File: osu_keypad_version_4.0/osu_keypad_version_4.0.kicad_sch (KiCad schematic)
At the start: 28 parts, among them J1 AVR-ISP-6, SW1 SW_Push, U1 ATmega32U4-A, Y1 16Mhz

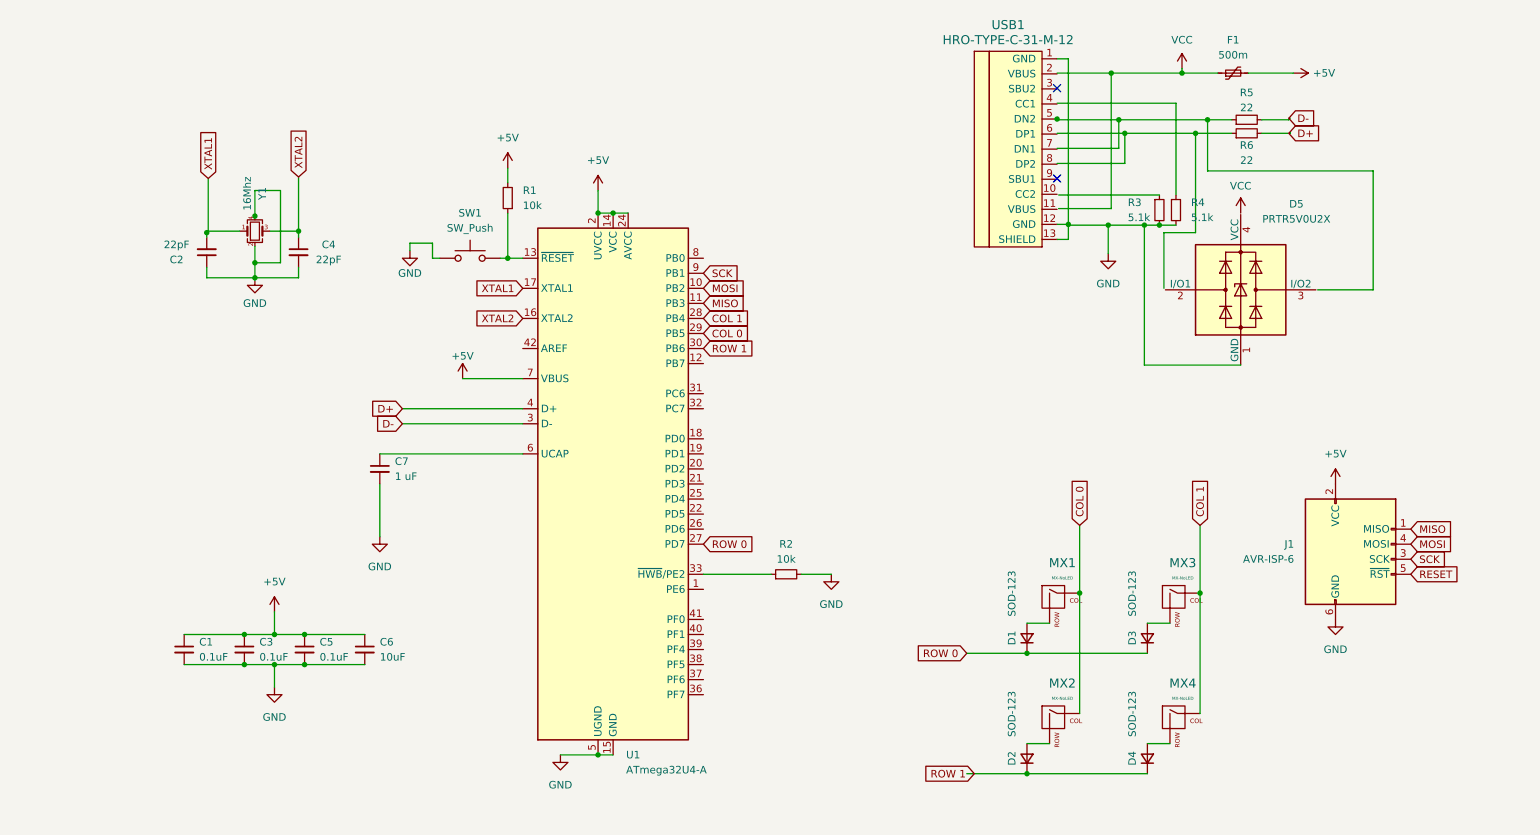
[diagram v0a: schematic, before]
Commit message: added rotary encoder
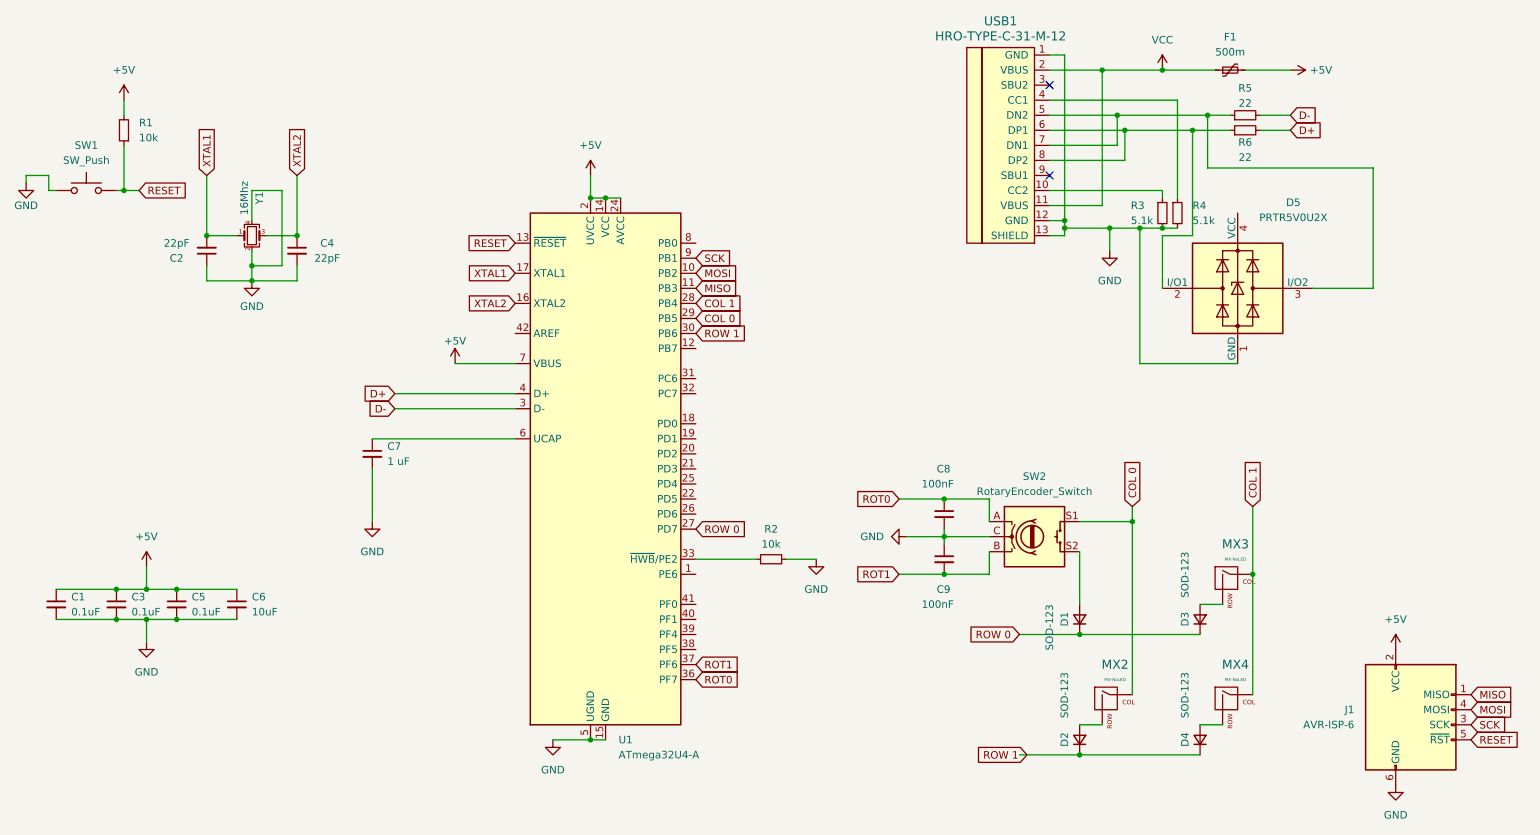
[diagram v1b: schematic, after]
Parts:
- removed MX1: MX-NoLED, MX_Alps_Hybrid:MX-1U-NoLED, symbol MX_Alps_Hybrid:MX-NoLED
- added C8, C9: 100nF, symbol Device:C_Small
- added SW2: RotaryEncoder_Switch, symbol Device:RotaryEncoder_Switch
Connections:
- net COL 0: now also SW2.S1
- net GND: now also R4.2, USB1.1 (GND), USB1.12 (GND), USB1.13 (SHIELD), C8.2, C9.1, SW2.C
- net RESET: now also R1.1, SW1.2, U1.13 (~{RESET})
- net VCC: now also USB1.11 (VBUS), USB1.2 (VBUS)
- net at R6.1: now also D5.2 (I/O1), USB1.6 (DP1), USB1.8 (DP2)
- net ROT0: now reaches U1.36 (PF7)
- net ROT0: now also C8.1, SW2.A
- net ROT1: now reaches U1.37 (PF6)
- net ROT1: now also C9.2, SW2.B
- net at R4.1: now also USB1.4 (CC1)
- net at R5.1, USB1.5 (DN2): now also D5.3 (I/O2), USB1.7 (DN1)
- net at R3.1: now also USB1.10 (CC2)
- net at D1.2 (A): now also SW2.S2
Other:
- moved on the sheet: C1, C3, C5, C6, C7, D1, D2, D3, D4, D5, F1, J1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

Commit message: added footprints
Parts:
- removed MX4: MX-NoLED, MX_Alps_Hybrid:MX-1U-NoLED, symbol MX_Alps_Hybrid:MX-NoLED
- added MX1: MX-NoLED, Alps_Only:ALPS-1U, symbol MX_Alps_Hybrid:MX-NoLED
- C1: renamed from C2; footprint Capacitor_SMD:C_0805_2012Metric -> Capacitor_SMD:C_0805_2012Metric_Pad1.18x1.45mm_HandSolder
- C2: renamed from C4; footprint Capacitor_SMD:C_0805_2012Metric -> Capacitor_SMD:C_0805_2012Metric_Pad1.18x1.45mm_HandSolder
- C3: renamed from C7; footprint Capacitor_SMD:C_0805_2012Metric -> Capacitor_SMD:C_0805_2012Metric_Pad1.18x1.45mm_HandSolder
- C4: renamed from C8; footprint (none) -> Capacitor_SMD:C_0805_2012Metric_Pad1.18x1.45mm_HandSolder
- C5: renamed from C9; footprint (none) -> Capacitor_SMD:C_0805_2012Metric_Pad1.18x1.45mm_HandSolder
- C6: renamed from C1; footprint Capacitor_SMD:C_0805_2012Metric -> Capacitor_SMD:C_0805_2012Metric_Pad1.18x1.45mm_HandSolder
- C7: renamed from C3; footprint Capacitor_SMD:C_0805_2012Metric -> Capacitor_SMD:C_0805_2012Metric_Pad1.18x1.45mm_HandSolder
- C8: renamed from C5; footprint Capacitor_SMD:C_0805_2012Metric -> Capacitor_SMD:C_0805_2012Metric_Pad1.18x1.45mm_HandSolder
- C9: renamed from C6; footprint Capacitor_SMD:C_0805_2012Metric -> Capacitor_SMD:C_0805_2012Metric_Pad1.18x1.45mm_HandSolder
- D1: renamed from D5; footprint Package_TO_SOT_SMD:SOT-143 -> random-keyboard-parts:SOT143B
- F1: value 500m -> 500mA; footprint (none) -> Fuse:Fuse_1206_3216Metric_Pad1.42x1.75mm_HandSolder
- J1: footprint (none) -> random-keyboard-parts:Reset_Pretty-Mask
- MX2, MX3: footprint MX_Alps_Hybrid:MX-1U-NoLED -> Alps_Only:ALPS-1U
- R1: renamed from R5; footprint (none) -> Resistor_SMD:R_0805_2012Metric_Pad1.20x1.40mm_HandSolder
- R2: renamed from R1; footprint Resistor_SMD:R_0805_2012Metric -> Resistor_SMD:R_0805_2012Metric_Pad1.20x1.40mm_HandSolder
- R3: renamed from R6; footprint (none) -> Resistor_SMD:R_0805_2012Metric_Pad1.20x1.40mm_HandSolder
- R4: renamed from R3; footprint (none) -> Resistor_SMD:R_0805_2012Metric_Pad1.20x1.40mm_HandSolder
- R5: renamed from R4; footprint (none) -> Resistor_SMD:R_0805_2012Metric_Pad1.20x1.40mm_HandSolder
- SW1: footprint random-keyboard-parts:SKQG-1155865 -> Button_Switch_SMD:SW_SPST_SKQG_WithStem
- SW2: footprint (none) -> Rotary_Encoder:RotaryEncoder_Alps_EC12E-Switch_Vertical_H20mm
- USB1: footprint (none) -> Type-C:HRO-TYPE-C-31-M-12-HandSoldering
- Y1: footprint Crystal:Crystal_SMD_3225-4Pin_3.2x2.5mm -> Crystal:Crystal_SMD_3225-4Pin_3.2x2.5mm_HandSoldering
- renumbered D1 to D2, D2 to D4, D4 to D5, R2 to R6
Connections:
- net COL 0: now also MX3.1 (COL), U1.28 (PB4); no longer MX2.1 (COL), U1.29 (PB5)
- net COL 1: now also MX2.1 (COL), U1.29 (PB5), MX1.1 (COL); no longer MX3.1 (COL), U1.28 (PB4)
- net ROT0: now also U1.31 (PC6); no longer U1.36 (PF7)
- net ROT1: now also U1.32 (PC7); no longer U1.37 (PF6)
- net ROW 0: now also U1.1 (PE6); no longer U1.27 (PD7)
- net ROW 1: now also U1.38 (PF5); no longer U1.30 (PB6)
- net VCC: now also D1.4 (VCC)
- net at MX2.2 (ROW): now also D5.2 (A); no longer D4.2 (A)
- net at D3.2 (A): now also MX1.2 (ROW); no longer MX3.2 (ROW)
- new net: D4.2 (A), MX3.2 (ROW)
- no-connect marks 2 -> 19
